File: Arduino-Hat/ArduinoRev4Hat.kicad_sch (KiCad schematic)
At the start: 11 parts, among them J1 Conn_01x10_Pin, J10 73099-0, J11 73099-0, J2 Conn_01x08_Pin, J3 Conn_01x04_Pin, J4 Conn_01x04_Pin, J5 Conn_01x04_Pin, J6 73099-0, J7 73099-0, J8 73099-0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

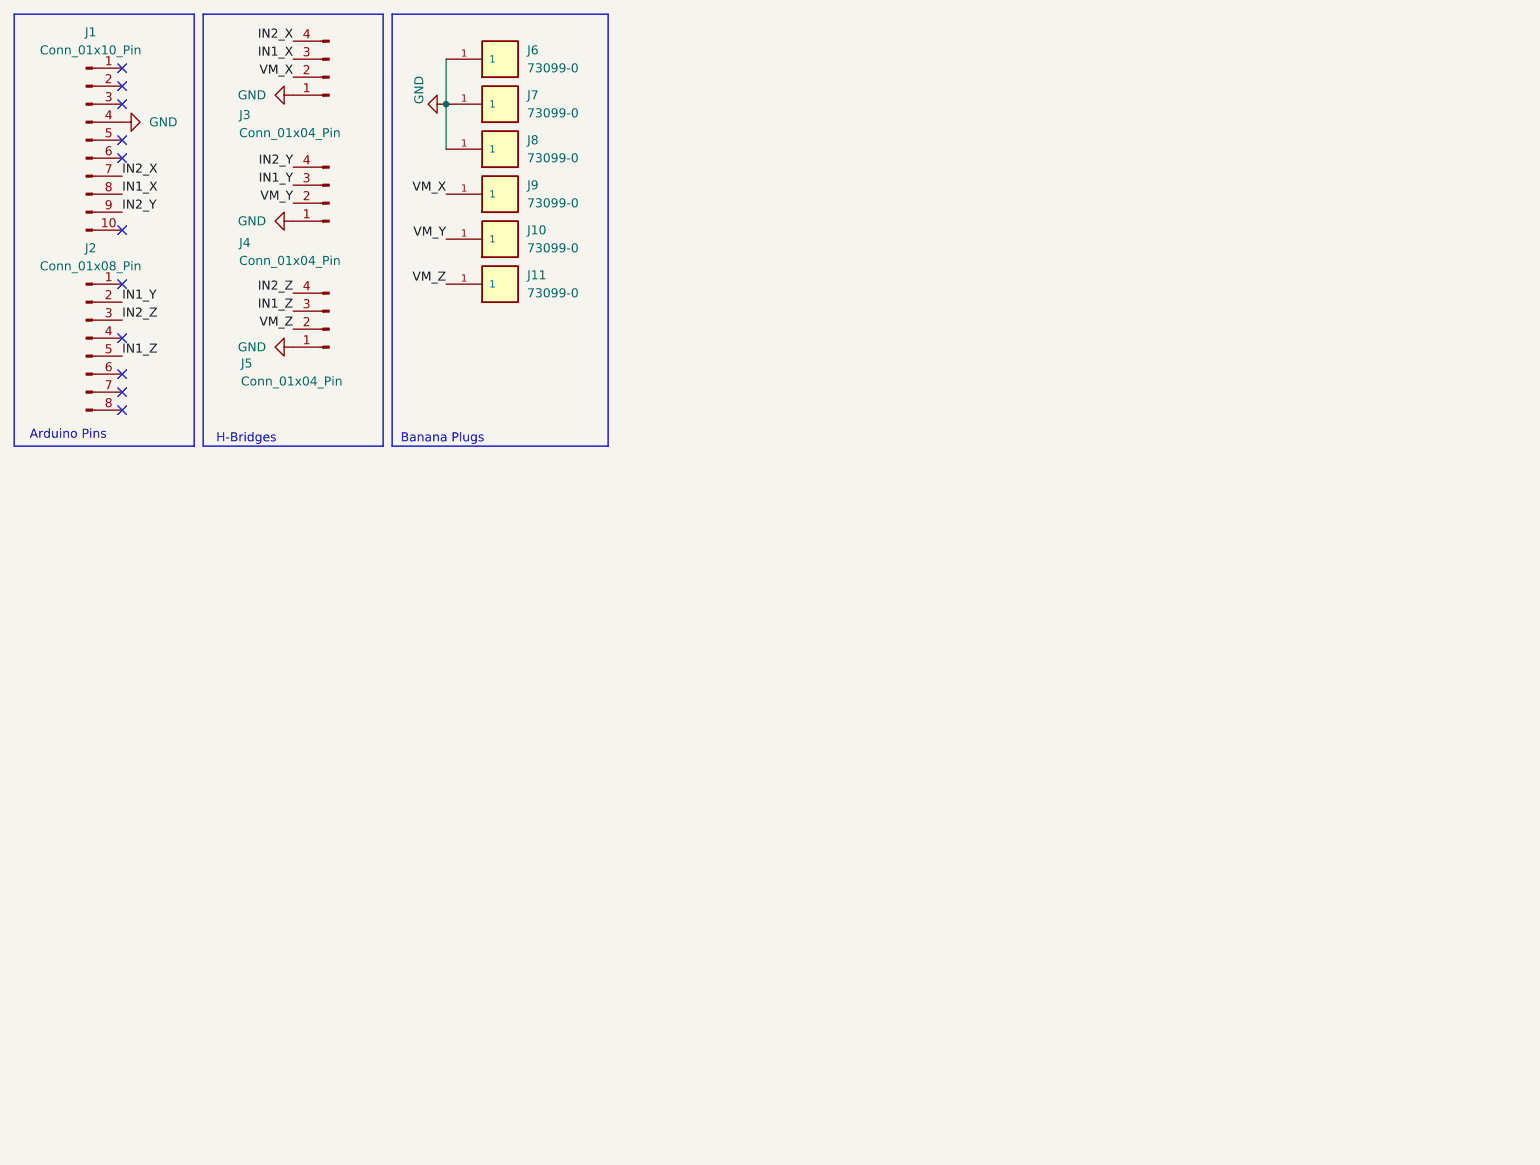
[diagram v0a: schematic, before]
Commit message: finailzied prototype for the magnetometer pcb
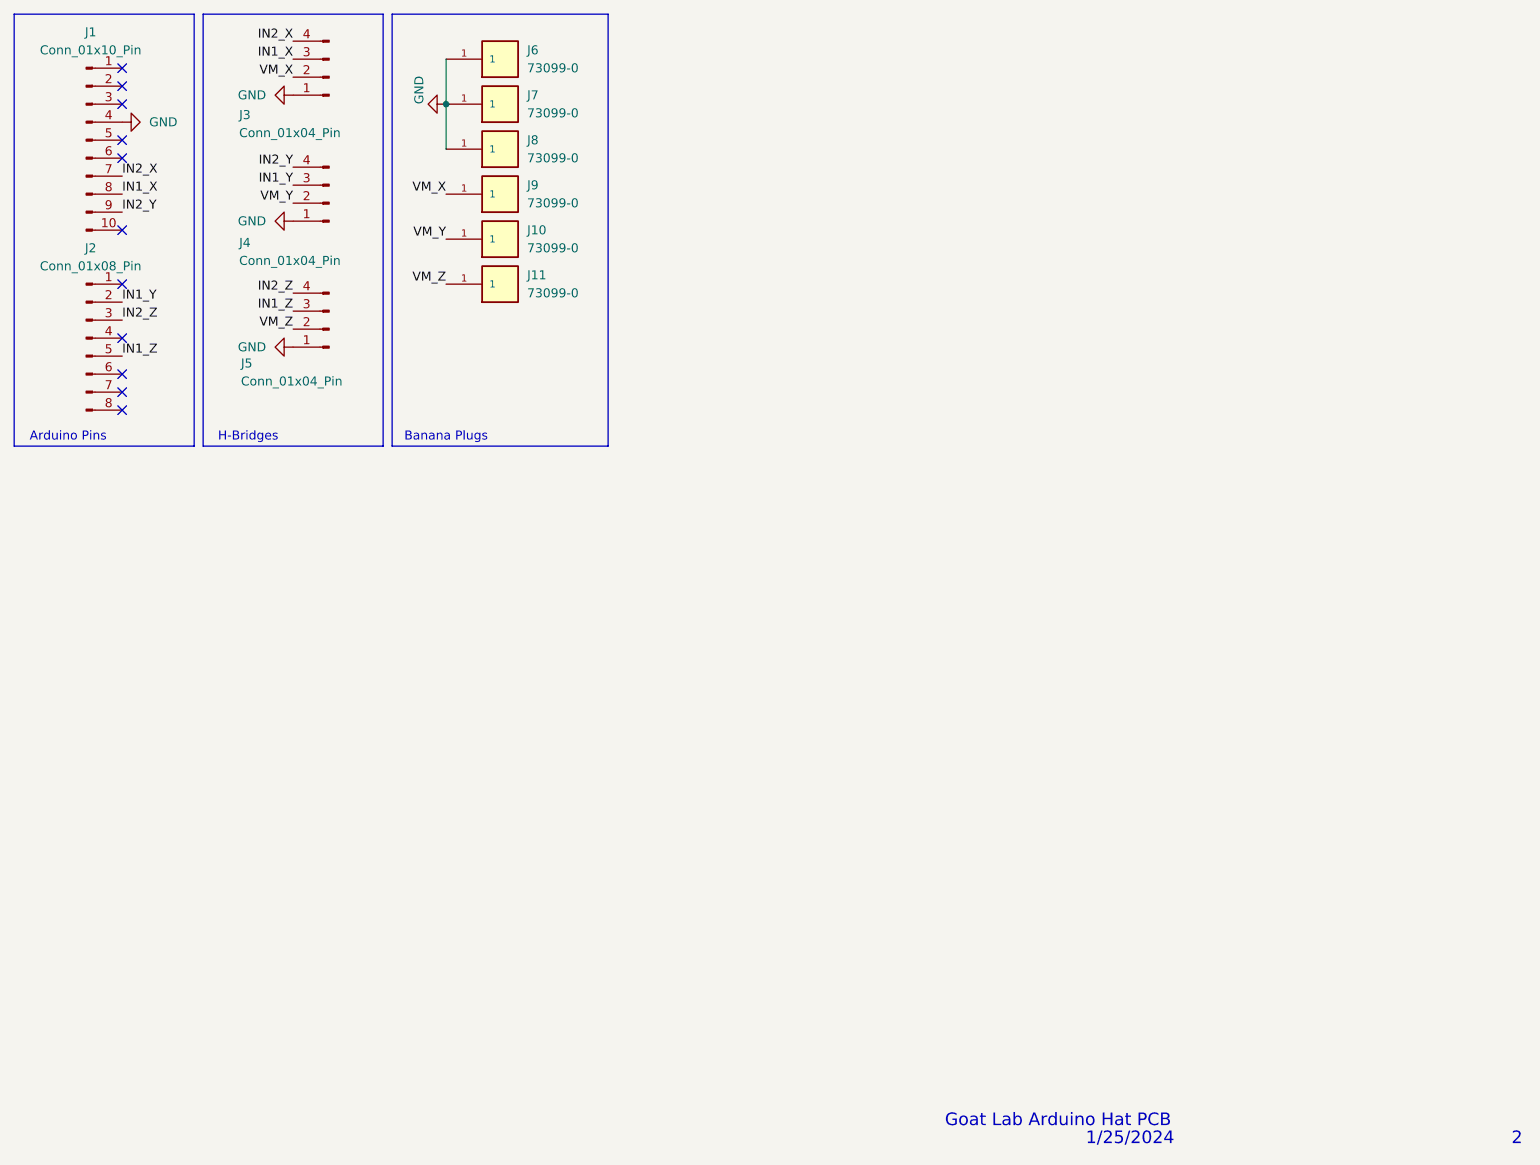
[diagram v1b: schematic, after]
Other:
- note added: "1/25/2024"
- note added: "2"
- note added: "Goat Lab Arduino Hat PCB"
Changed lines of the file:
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@@
 	(text "H-Bridges"
 		(exclude_from_sim no)
-		(at 89.916 94.234 0)
+		(at 90.17 93.98 0)
 		(effects
 			(font
@@
 		)
 	)
+	(text "Goat Lab Arduino Hat PCB"
+		(exclude_from_sim no)
+		(at 204.47 190.5 0)
+		(effects
+			(font
+				(size 1.778 1.778)
+			)
+		)
+	)
 	(text "Banana Plugs"
 		(exclude_from_sim no)
-		(at 117.602 94.234 0)
+		(at 118.11 93.98 0)
 		(effects
 			(font
@@
 	(text "Arduino Pins"
 		(exclude_from_sim no)
-		(at 64.77 93.726 0)
+		(at 64.77 93.98 0)
 		(effects
 			(font
@@
 			)
 		)
+	)
+	(text "1/25/2024"
+		(exclude_from_sim no)
+		(at 214.63 193.04 0)
+		(effects
+			(font
+				(size 1.778 1.778)
+			)
+		)
+	)
+	(text "2"
+		(exclude_from_sim no)
+		(at 269.24 193.04 0)
+		(effects
+			(font
+				(size 1.778 1.778)
+			)
+		)

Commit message: newest version
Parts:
- renumbered J7 to J10, J8 to J11, J11 to J6, J9 to J7, J10 to J8, J6 to J9
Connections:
- net IN1_X: now also J5.3 (Pin_3); no longer J3.3 (Pin_3)
- net IN1_Z: now also J3.3 (Pin_3); no longer J5.3 (Pin_3)
- net IN2_X: now also J5.4 (Pin_4); no longer J3.4 (Pin_4)
- net IN2_Z: now also J3.4 (Pin_4); no longer J5.4 (Pin_4)
- net VM_X: now also J5.2 (Pin_2), J6.1; no longer J3.2 (Pin_2), J7.1
- net VM_Z: now also J3.2 (Pin_2), J7.1; no longer J5.2 (Pin_2), J6.1
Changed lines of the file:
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@@
 		)
 	)
-	(label "VM_X"
+	(label "VM_Z"
 		(at 118.11 59.69 180)
 		(fields_autoplaced yes)
@@
 		)
 	)
-	(label "VM_Z"
+	(label "VM_X"
 		(at 96.52 78.74 180)
 		(fields_autoplaced yes)
@@
 		)
 	)
-	(label "IN1_Z"
+	(label "IN1_X"
 		(at 96.52 76.2 180)
 		(fields_autoplaced yes)
@@
 		)
 	)
-	(label "VM_Z"
+	(label "VM_X"
 		(at 118.11 72.39 180)
 		(fields_autoplaced yes)
@@
 		)
 	)
-	(label "IN2_X"
+	(label "IN2_Z"
 		(at 96.52 38.1 180)
 		(fields_autoplaced yes)
@@
 		)
 	)
-	(label "VM_X"
+	(label "VM_Z"
 		(at 96.52 43.18 180)
 		(fields_autoplaced yes)
@@
 		)
 	)
-	(label "IN2_Z"
+	(label "IN2_X"
 		(at 96.52 73.66 180)
 		(fields_autoplaced yes)
@@
 		)
 	)
-	(label "IN1_X"
+	(label "IN1_Z"
 		(at 96.52 40.64 180)
 		(fields_autoplaced yes)
@@
 		(dnp no)
 		(fields_autoplaced yes)
-		(property "Reference" "J11"
+		(property "Reference" "J6"
 			(at 129.54 71.1199 0)
 			(effects
@@
 			(project "ArduinoRev4Hat"
 				(path "/3cd5f95e-5b22-4342-86a1-cdbd217d3c5d"
-					(reference "J11")
+					(reference "J6")
 					(unit 1)
 				)
@@
 		(dnp no)
 		(fields_autoplaced yes)
-		(property "Reference" "J6"
+		(property "Reference" "J9"
 			(at 129.54 39.3699 0)
 			(effects
@@
 			(project ""
 				(path "/3cd5f95e-5b22-4342-86a1-cdbd217d3c5d"
-					(reference "J6")
+					(reference "J9")
 					(unit 1)
 				)
@@
 		(dnp no)
 		(fields_autoplaced yes)
-		(property "Reference" "J10"
+		(property "Reference" "J8"
 			(at 129.54 64.7699 0)
 			(effects
@@
 			(project "ArduinoRev4Hat"
 				(path "/3cd5f95e-5b22-4342-86a1-cdbd217d3c5d"
-					(reference "J10")
+					(reference "J8")
 					(unit 1)
 				)
@@
 		(dnp no)
 		(fields_autoplaced yes)
-		(property "Reference" "J8"
+		(property "Reference" "J11"
 			(at 129.54 52.0699 0)
 			(effects
@@
 			(project "ArduinoRev4Hat"
 				(path "/3cd5f95e-5b22-4342-86a1-cdbd217d3c5d"
-					(reference "J8")
+					(reference "J11")
 					(unit 1)
 				)
@@
 		(dnp no)
 		(fields_autoplaced yes)
-		(property "Reference" "J9"
+		(property "Reference" "J7"
 			(at 129.54 58.4199 0)
 			(effects
@@
 			(project "ArduinoRev4Hat"
 				(path "/3cd5f95e-5b22-4342-86a1-cdbd217d3c5d"
-					(reference "J9")
+					(reference "J7")
 					(unit 1)
 				)
@@
 		(dnp no)
 		(fields_autoplaced yes)
-		(property "Reference" "J7"
+		(property "Reference" "J10"
 			(at 129.54 45.7199 0)
 			(effects
@@
 			(project "ArduinoRev4Hat"
 				(path "/3cd5f95e-5b22-4342-86a1-cdbd217d3c5d"
-					(reference "J7")
+					(reference "J10")
 					(unit 1)
 				)
